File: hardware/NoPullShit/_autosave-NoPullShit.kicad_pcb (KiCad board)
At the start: 2 copper layers, 52 parts, among them J1 USB Power, J2 Load cell, J3 Batt+, J4 Batt-, J5 ICSP, J6 UART, J7 Spk+, J8 Spk-, Q1 BC808, Q1 S8550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

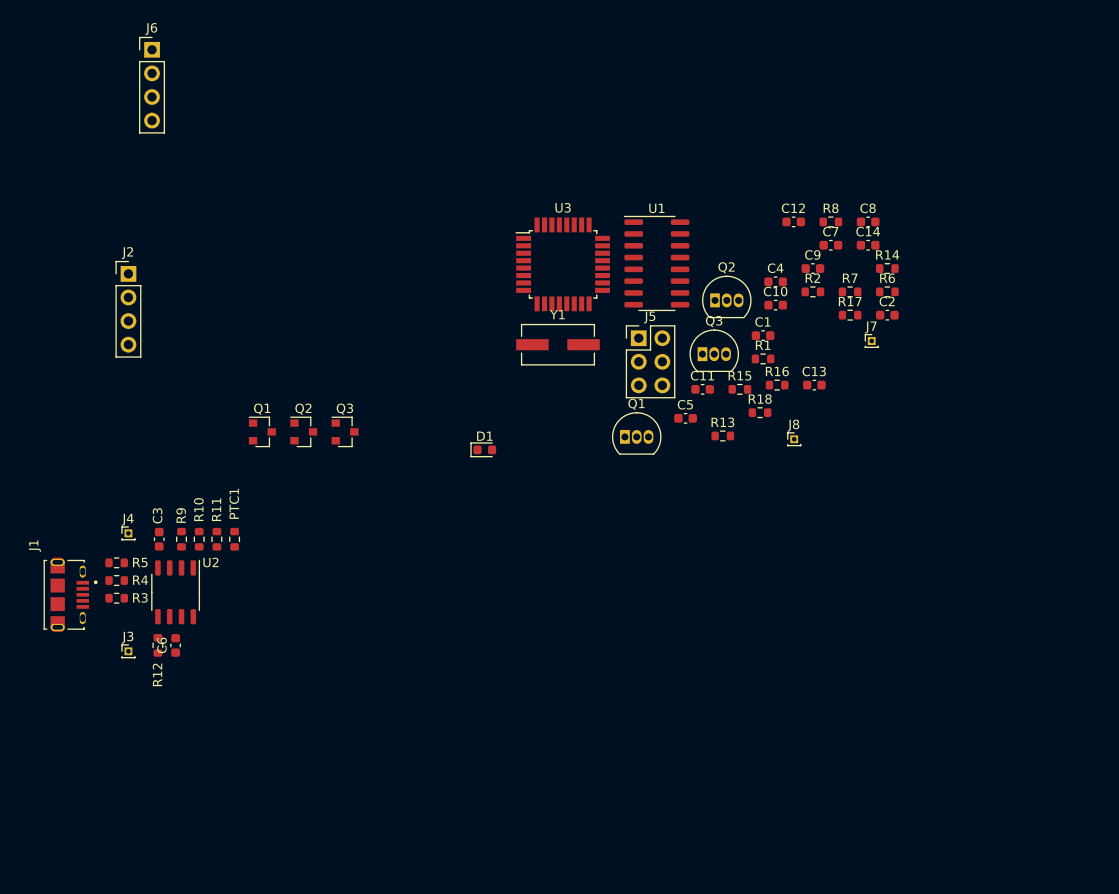
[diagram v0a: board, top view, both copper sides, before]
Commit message: Footprint assignment + initial grouping
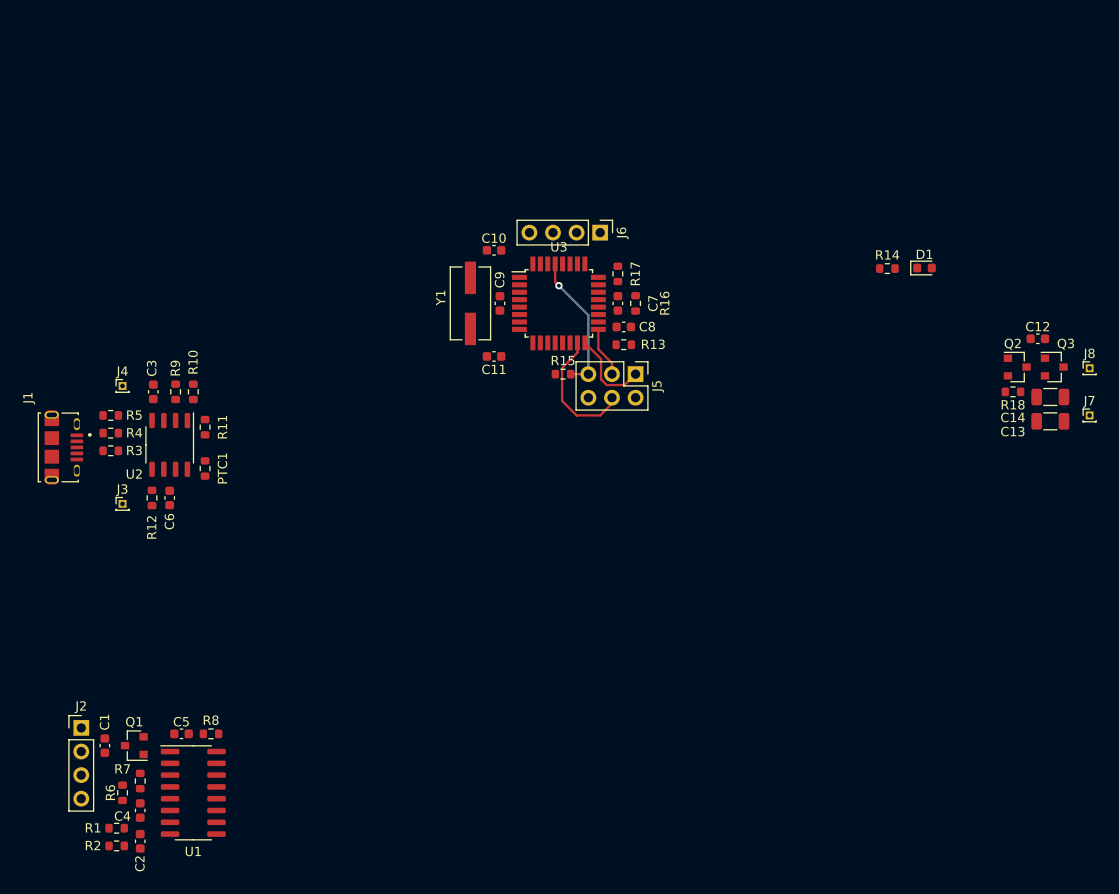
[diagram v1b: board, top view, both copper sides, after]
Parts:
- removed the Q1 at (72.5, 67.1)
- removed the Q2 at (82.2, 52.4)
- removed the Q3 at (80.9, 58.2)
- C13, C14: footprint Capacitor_SMD:C_0603_1608Metric -> Capacitor_SMD:C_1206_3216Metric
- moved R6 98.5 mm to (18.4, 105.4), turned to 270 degrees
- moved C2 98.4 mm to (20.3, 110.6), turned to 90 degrees
- moved R2 95.8 mm to (17.8, 111.1), turned to 180 degrees
- moved R7 92.8 mm to (20.3, 104.1), turned to 270 degrees
- moved C4 89.0 mm to (20.3, 107.3), turned to 270 degrees
- moved R8 86.6 mm to (27.9, 99.1)
- moved R1 86.0 mm to (17.8, 109.2), turned to 180 degrees
- moved C1 83.5 mm to (16.5, 100.3), turned to 270 degrees
- moved Q2 77.2 mm to (114.8, 59.6)
- moved Q3 76.7 mm to (118.7, 59.6)
- moved U1 75.8 mm to (26.0, 105.4)
- moved C5 64.0 mm to (24.8, 99.1), turned to 180 degrees
- moved J6 52.1 mm to (69.8, 45.1), turned to 270 degrees
- moved D1 51.2 mm to (104.8, 48.9)
- moved J2 49.2 mm to (14.0, 98.4)
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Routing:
- net Net-(J5-Pad5): track 0.00 -> 15.3 mm, vias 0 -> 1
- net Net-(J5-Pad4): track 0.00 -> 14.1 mm
- net Net-(J5-Pad1): track 0.00 -> 9.11 mm
- net Net-(J5-Pad3): track 0.00 -> 5.43 mm
